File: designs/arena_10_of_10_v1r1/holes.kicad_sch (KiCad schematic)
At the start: 4 parts

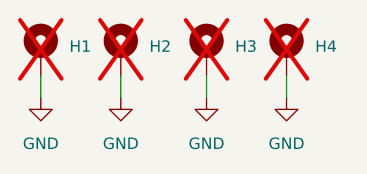
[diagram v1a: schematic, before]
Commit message: Resolved all DSR voilations in schematic.
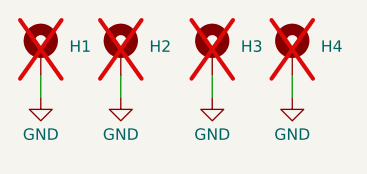
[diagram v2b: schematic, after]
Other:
- moved on the sheet: H3, H4
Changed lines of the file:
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@@
 	(wire
 		(pts
-			(xy 59.055 30.48) (xy 59.055 33.02)
+			(xy 59.69 30.48) (xy 59.69 33.02)
 		)
 		(stroke
@@
 	(wire
 		(pts
-			(xy 50.165 30.48) (xy 50.165 33.02)
+			(xy 50.8 30.48) (xy 50.8 33.02)
 		)
 		(stroke
@@
 	)
 	(symbol
+		(lib_name "GND_1")
 		(lib_id "power:GND")
 		(at 31.75 33.02 0)
-		(mirror y)
 		(unit 1)
 		(exclude_from_sim no)
@@
 		(on_board yes)
 		(dnp no)
-		(fields_autoplaced yes)
-		(property "Reference" "#PWR0333"
+		(property "Reference" "#PWR0264"
 			(at 31.75 39.37 0)
 			(effects
@@
 		)
 		(property "Value" "GND"
-			(at 31.75 38.1 0)
+			(at 31.75 37.084 0)
 			(effects
 				(font
@@
 			)
 		)
-		(property "Description" ""
+		(property "Description" "Power symbol creates a global label with name \"GND\" , ground"
 			(at 31.75 33.02 0)
 			(effects
@@
 		)
 		(instances
-			(project "arena_10_of_10_v1r1"
-				(path "/056666d2-2c8f-491c-bcad-db3c517779a8/3f6f12ad-0207-48b9-8360-f583cf48d0a1"
-					(reference "#PWR0333")
+			(project ""
+				(path "/056666d2-2c8f-491c-bcad-db3c517779a8/3f6f12ad-0207-48b9-8360-f583cf48d0a1"
+					(reference "#PWR0264")
 					(unit 1)
 				)
@@
 	)
 	(symbol
+		(lib_name "GND_1")
+		(lib_id "power:GND")
+		(at 40.64 33.02 0)
+		(unit 1)
+		(exclude_from_sim no)
+		(in_bom yes)
+		(on_board yes)
+		(dnp no)
+		(property "Reference" "#PWR0265"
+			(at 40.64 39.37 0)
+			(effects
+				(font
+					(size 1.27 1.27)
+				)
+				(hide yes)
+			)
+		)
+		(property "Value" "GND"
+			(at 40.64 37.084 0)
+			(effects
+				(font
+					(size 1.27 1.27)
+				)
+			)
+		)
+		(property "Footprint" ""
+			(at 40.64 33.02 0)
+			(effects
+				(font
+					(size 1.27 1.27)
+				)
+				(hide yes)
+			)
+		)
+		(property "Datasheet" ""
+			(at 40.64 33.02 0)
+			(effects
+				(font
+					(size 1.27 1.27)
+				)
+				(hide yes)
+			)
+		)
+		(property "Description" "Power symbol creates a global label with name \"GND\" , ground"
+			(at 40.64 33.02 0)
+			(effects
+				(font
+					(size 1.27 1.27)
+				)
+				(hide yes)
+			)
+		)
+		(pin "1"
+		)
+		(instances
+			(project "arena_10_of_10_v1r1"
+				(path "/056666d2-2c8f-491c-bcad-db3c517779a8/3f6f12ad-0207-48b9-8360-f583cf48d0a1"
+					(reference "#PWR0265")
+					(unit 1)
+				)
+			)
+		)
+	)
+	(symbol
+		(lib_name "GND_1")
+		(lib_id "power:GND")
+		(at 59.69 33.02 0)
+		(unit 1)
+		(exclude_from_sim no)
+		(in_bom yes)
+		(on_board yes)
+		(dnp no)
+		(property "Reference" "#PWR0269"
+			(at 59.69 39.37 0)
+			(effects
+				(font
+					(size 1.27 1.27)
+				)
+				(hide yes)
+			)
+		)
+		(property "Value" "GND"
+			(at 59.69 37.084 0)
+			(effects
+				(font
+					(size 1.27 1.27)
+				)
+			)
+		)
+		(property "Footprint" ""
+			(at 59.69 33.02 0)
+			(effects
+				(font
+					(size 1.27 1.27)
+				)
+				(hide yes)
+			)
+		)
+		(property "Datasheet" ""
+			(at 59.69 33.02 0)
+			(effects
+				(font
+					(size 1.27 1.27)
+				)
+				(hide yes)
+			)
+		)
+		(property "Description" "Power symbol creates a global label with name \"GND\" , ground"
+			(at 59.69 33.02 0)
+			(effects
+				(font
+					(size 1.27 1.27)
+				)
+				(hide yes)
+			)
+		)
+		(pin "1"
+		)
+		(instances
+			(project "arena_10_of_10_v1r1"
+				(path "/056666d2-2c8f-491c-bcad-db3c517779a8/3f6f12ad-0207-48b9-8360-f583cf48d0a1"
+					(reference "#PWR0269")
+					(unit 1)
+				)
+			)
+		)
+	)
+	(symbol
 		(lib_id "Mechanical:MountingHole_Pad")
-		(at 50.165 27.94 0)
+		(at 50.8 27.94 0)
 		(unit 1)
 		(exclude_from_sim no)
@@
 		(fields_autoplaced yes)
 		(property "Reference" "H3"
-			(at 53.34 27.305 0)
+			(at 53.975 27.305 0)
 			(effects
 				(font
@@
 		)
 		(property "Value" "MountingHole_Pad"
-			(at 53.34 28.575 0)
+			(at 53.975 28.575 0)
 			(effects
 				(font
@@
 		)
 		(property "Footprint" "MountingHole:MountingHole_4.5mm_Pad"
-			(at 50.165 27.94 0)
+			(at 50.8 27.94 0)
 			(effects
 				(font
@@
 		)
 		(property "Datasheet" "~"
-			(at 50.165 27.94 0)
+			(at 50.8 27.94 0)
 			(effects
 				(font
@@
 		)
 		(property "Description" ""
-			(at 50.165 27.94 0)
+			(at 50.8 27.94 0)
 			(effects
 				(font
@@
 	)
 	(symbol
+		(lib_name "GND_1")
 		(lib_id "power:GND")
-		(at 59.055 33.02 0)
-		(mirror y)
+		(at 50.8 33.02 0)
 		(unit 1)
 		(exclude_from_sim no)
@@
 		(on_board yes)
 		(dnp no)
-		(fields_autoplaced yes)
-		(property "Reference" "#PWR0336"
-			(at 59.055 39.37 0)
+		(property "Reference" "#PWR0268"
+			(at 50.8 39.37 0)
 			(effects
 				(font
@@
 		)
 		(property "Value" "GND"
-			(at 59.055 38.1 0)
+			(at 50.8 37.084 0)
 			(effects
 				(font
@@
 		)
 		(property "Footprint" ""
-			(at 59.055 33.02 0)
+			(at 50.8 33.02 0)
 			(effects
 				(font
@@
 		)
 		(property "Datasheet" ""
-			(at 59.055 33.02 0)
-			(effects
-				(font
-					(size 1.27 1.27)
-				)
-				(hide yes)
-			)
-		)
-		(property "Description" ""
-			(at 59.055 33.02 0)
+			(at 50.8 33.02 0)
+			(effects
+				(font
+					(size 1.27 1.27)
+				)
+				(hide yes)
+			)
+		)
+		(property "Description" "Power symbol creates a global label with name \"GND\" , ground"
+			(at 50.8 33.02 0)
 			(effects
 				(font
@@
 			(project "arena_10_of_10_v1r1"
 				(path "/056666d2-2c8f-491c-bcad-db3c517779a8/3f6f12ad-0207-48b9-8360-f583cf48d0a1"
-					(reference "#PWR0336")
-					(unit 1)
-				)
-			)
-		)
-	)
-	(symbol
-		(lib_id "power:GND")
-		(at 50.165 33.02 0)
-		(mirror y)
-		(unit 1)
-		(exclude_from_sim no)
-		(in_bom yes)
-		(on_board yes)
-		(dnp no)
-		(fields_autoplaced yes)
-		(property "Reference" "#PWR0335"
-			(at 50.165 39.37 0)
-			(effects
-				(font
-					(size 1.27 1.27)
-				)
-				(hide yes)
-			)
-		)
-		(property "Value" "GND"
-			(at 50.165 38.1 0)
-			(effects
-				(font
-					(size 1.27 1.27)
-				)
-			)
-		)
-		(property "Footprint" ""
-			(at 50.165 33.02 0)
-			(effects
-				(font
-					(size 1.27 1.27)
-				)
-				(hide yes)
-			)
-		)
-		(property "Datasheet" ""
-			(at 50.165 33.02 0)
-			(effects
-				(font
-					(size 1.27 1.27)
-				)
-				(hide yes)
-			)
-		)
-		(property "Description" ""
-			(at 50.165 33.02 0)
-			(effects
-				(font
-					(size 1.27 1.27)
-				)
-				(hide yes)
-			)
-		)
-		(pin "1"
-		)
-		(instances
-			(project "arena_10_of_10_v1r1"
-				(path "/056666d2-2c8f-491c-bcad-db3c517779a8/3f6f12ad-0207-48b9-8360-f583cf48d0a1"
-					(reference "#PWR0335")
-					(unit 1)
-				)
-			)
-		)
-	)
-	(symbol
-		(lib_id "power:GND")
-		(at 40.64 33.02 0)
-		(mirror y)
-		(unit 1)
-		(exclude_from_sim no)
-		(in_bom yes)
-		(on_board yes)
-		(dnp no)
-		(fields_autoplaced yes)
-		(property "Reference" "#PWR0334"
-			(at 40.64 39.37 0)
-			(effects
-				(font
-					(size 1.27 1.27)
-				)
-				(hide yes)
-			)
-		)
-		(property "Value" "GND"
-			(at 40.64 38.1 0)
-			(effects
-				(font
-					(size 1.27 1.27)
-				)
-			)
-		)
-		(property "Footprint" ""
-			(at 40.64 33.02 0)
-			(effects
-				(font
-					(size 1.27 1.27)
-				)
-				(hide yes)
-			)
-		)
-		(property "Datasheet" ""
-			(at 40.64 33.02 0)
-			(effects
-				(font
-					(size 1.27 1.27)
-				)
-				(hide yes)
-			)
-		)
-		(property "Description" ""
-			(at 40.64 33.02 0)
-			(effects
-				(font
-					(size 1.27 1.27)
-				)
-				(hide yes)
-			)
-		)
-		(pin "1"
-		)
-		(instances
-			(project "arena_10_of_10_v1r1"
-				(path "/056666d2-2c8f-491c-bcad-db3c517779a8/3f6f12ad-0207-48b9-8360-f583cf48d0a1"
-					(reference "#PWR0334")
+					(reference "#PWR0268")
 					(unit 1)
 				)
@@
 	(symbol
 		(lib_id "Mechanical:MountingHole_Pad")
-		(at 59.055 27.94 0)
+		(at 59.69 27.94 0)
 		(unit 1)
 		(exclude_from_sim no)
@@
 		(fields_autoplaced yes)
 		(property "Reference" "H4"
-			(at 62.23 27.305 0)
+			(at 62.865 27.305 0)
 			(effects
 				(font
@@
 		)
 		(property "Value" "MountingHole_Pad"
-			(at 62.23 28.575 0)
+			(at 62.865 28.575 0)
 			(effects
 				(font
@@
 		)
 		(property "Footprint" "MountingHole:MountingHole_4.5mm_Pad"
-			(at 59.055 27.94 0)
+			(at 59.69 27.94 0)
 			(effects
 				(font
@@
 		)
 		(property "Datasheet" "~"
-			(at 59.055 27.94 0)
+			(at 59.69 27.94 0)
 			(effects
 				(font
@@
 		)
 		(property "Description" ""
-			(at 59.055 27.94 0)
-			(effects
-				(font
+			(at 59.69 27.94 0)
+			(effects
+				(font
